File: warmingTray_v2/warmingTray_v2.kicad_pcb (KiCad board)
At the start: 2 copper layers, 37 parts, among them J1 Jack-DC, P1 Power, P2 Analog, P3 Analog, P4 Digital, P5 PWM, P6 PWM, P7 Communication

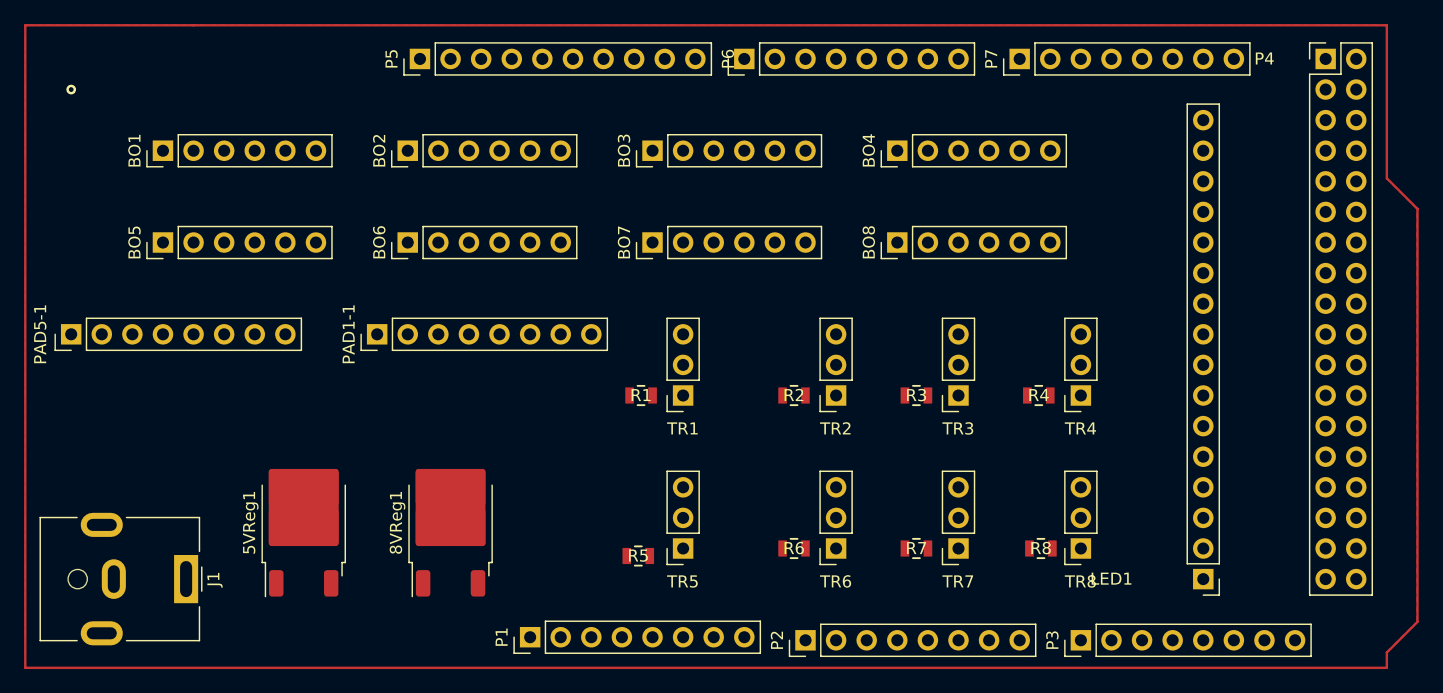
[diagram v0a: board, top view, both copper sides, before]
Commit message: added traces to pcb
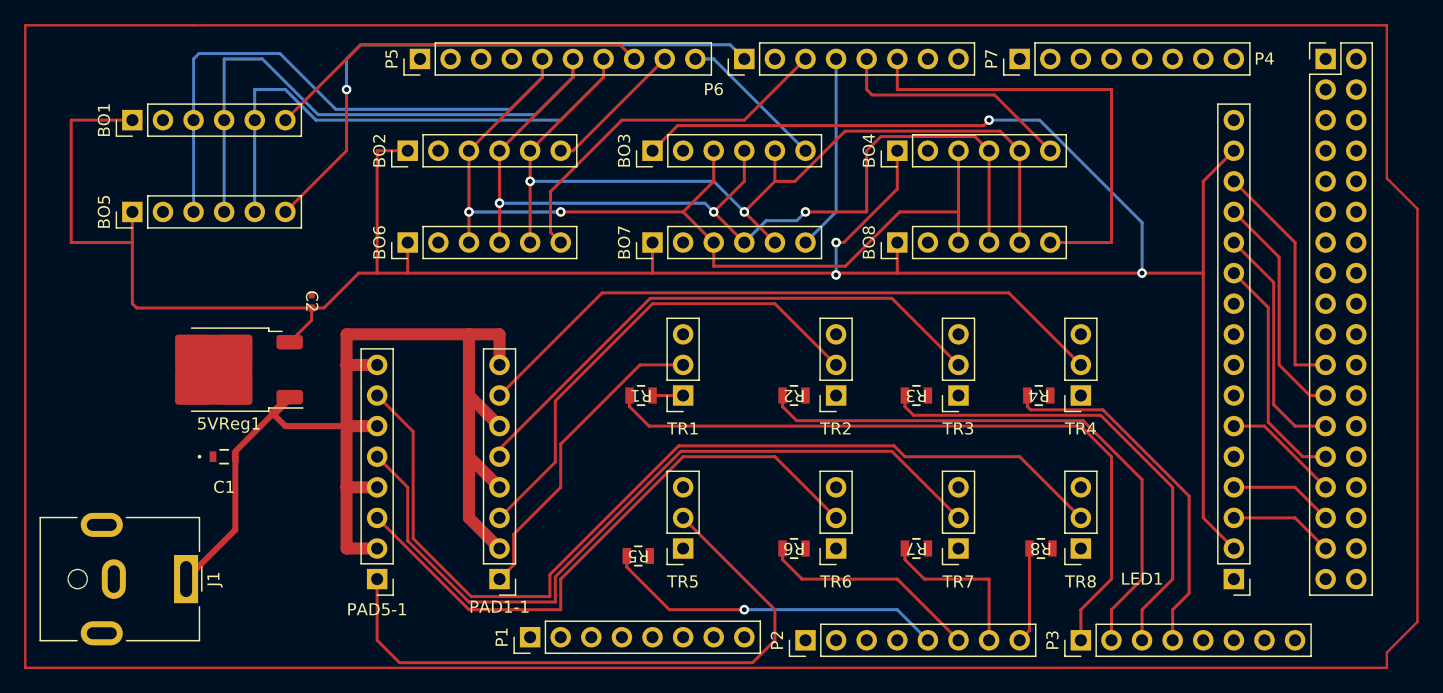
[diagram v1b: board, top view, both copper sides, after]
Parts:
- removed 8VReg1: LM78M05_TO252, Package_TO_SOT_SMD:TO-252-2
- added C1: C, footprints_0-33uF:CAP_1608_TDK, F.Cu at (116.8, 104.1)
- added C2: C, footprints_0-1uF_Capacitor:CAP_CL05_SAM, F.Cu at (124.1, 91.2)
- moved PAD5-1 32.5 mm to (129.5, 114.3), turned to 180 degrees
- moved PAD1-1 22.7 mm to (139.7, 114.3), turned to 180 degrees
- moved 5VReg1 14.1 mm to (117.2, 96.9), turned to 180 degrees
- moved BO5 3.59 mm to (109.2, 83.8)
- moved BO1 3.59 mm to (109.2, 76.2)
- moved LED1 2.54 mm to (200.7, 114.3)
- turned R1 to 180 degrees
- turned R2 to 180 degrees
- turned R3 to 180 degrees
- turned R4 to 180 degrees
- turned R5 to 180 degrees
- turned R6 to 180 degrees
- turned R7 to 180 degrees
- turned R8 to 180 degrees
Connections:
- BO4 pad 6: /7(**) -> /3(**)
- BO5 pad 6: /6(**) -> /7(**)
- BO8 pad 6: /3(**) -> /2(**)
- R1 pad 2: /A0 -> /A8
- R2 pad 2: /A1 -> /A9
- R3 pad 2: /A2 -> /A10
- R4 pad 2: /A3 -> /A11
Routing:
- net /VCC5: track 0.00 -> 239.4 mm, vias 0 -> 4
- net /12(**): track 0.00 -> 127.0 mm, vias 0 -> 3
- net /13(**): track 0.00 -> 123.4 mm, vias 0 -> 2
- net /11(**): track 0.00 -> 119.8 mm, vias 0 -> 2
- net +12V: track 0.00 -> 94.4 mm
- net /Pad8: track 0.00 -> 79.3 mm
- net /Pad7: track 0.00 -> 64.6 mm
- net /A8: track 0.00 -> 58.9 mm
- net /Pad4: track 0.00 -> 54.3 mm
- net /Pad5: track 0.00 -> 53.0 mm
- net /Pad6: track 0.00 -> 50.1 mm
- net /7(**): track 0.00 -> 48.8 mm, vias 0 -> 1
- net /A9: track 0.00 -> 47.7 mm
- net /Pad3: track 0.00 -> 46.2 mm
- net /Pad2: track 0.00 -> 40.4 mm
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
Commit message: updated resistor footprint
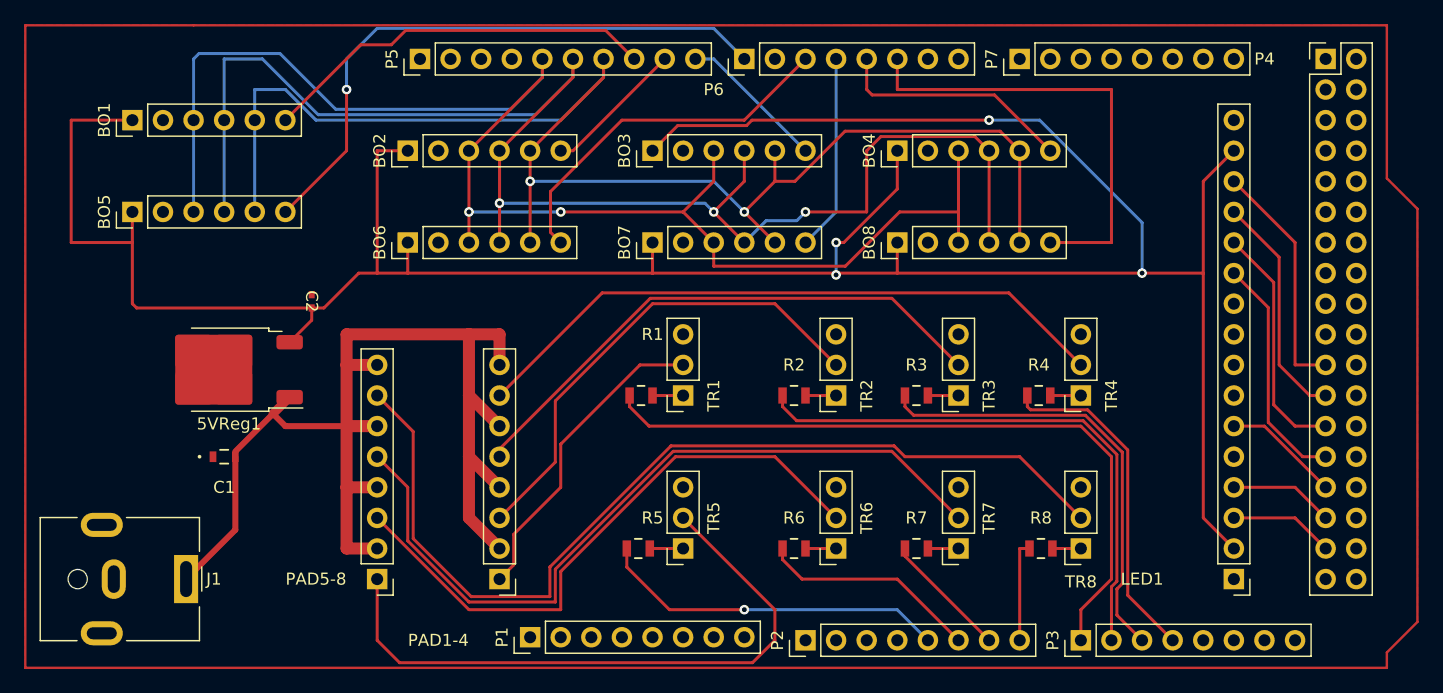
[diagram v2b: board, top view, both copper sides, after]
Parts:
- moved R5 0.62 mm to (151.2, 111.8)
- renumbered PAD1-1 to PAD1-4, PAD5-1 to PAD5-8
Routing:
- net /A6: track 13.7 -> 10.5 mm
- net Net-(TR5-Pin_1): track 0.00 -> 2.77 mm
- net Net-(TR7-Pin_1): track 0.00 -> 2.54 mm
- net Net-(TR4-Pin_1): track 0.00 -> 2.54 mm
- net Net-(TR3-Pin_1): track 0.00 -> 2.54 mm
- net Net-(TR6-Pin_1): track 0.00 -> 2.54 mm
- net Net-(TR2-Pin_1): track 0.00 -> 2.54 mm
- net /A10: track 39.7 -> 37.2 mm
- net Net-(TR8-Pin_1): track 0.00 -> 2.36 mm
- net /A11: track 30.0 -> 28.1 mm
- net /A9: track 47.7 -> 45.9 mm
- net /7(**): track 48.8 -> 49.9 mm
- net /10(**): track 32.0 -> 33.0 mm
- net /A4: track 28.4 -> 29.1 mm
